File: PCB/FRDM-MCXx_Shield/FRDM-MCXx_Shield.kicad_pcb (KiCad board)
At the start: 4 copper layers, 54.3 x 54.7 mm, 96 parts, among them J1 Conn_02x08_Odd_Even, J2 Conn_02x06_Odd_Even, J3 Conn_02x10_Odd_Even, J4 Conn_02x08_Odd_Even, J5 Conn_01x04_Socket, J6 Conn_01x04_Pin, J7 Conn_01x04_Pin, J8 Conn_01x04_Pin, M1 Motor_Servo, SW1 EC12D1524406, U1 74HC595, U2 M95010-RMN6TP, U3 LM35-D

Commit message: Updated PCB
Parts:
- removed the REF2 at (73.8, 258.9)
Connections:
- J2 pad 2: /ADC_OUT -> /LM35_V_OUT
- U3 pad 1: /ADC_OUT -> /Sensors & actuators/LM35_V_OUT

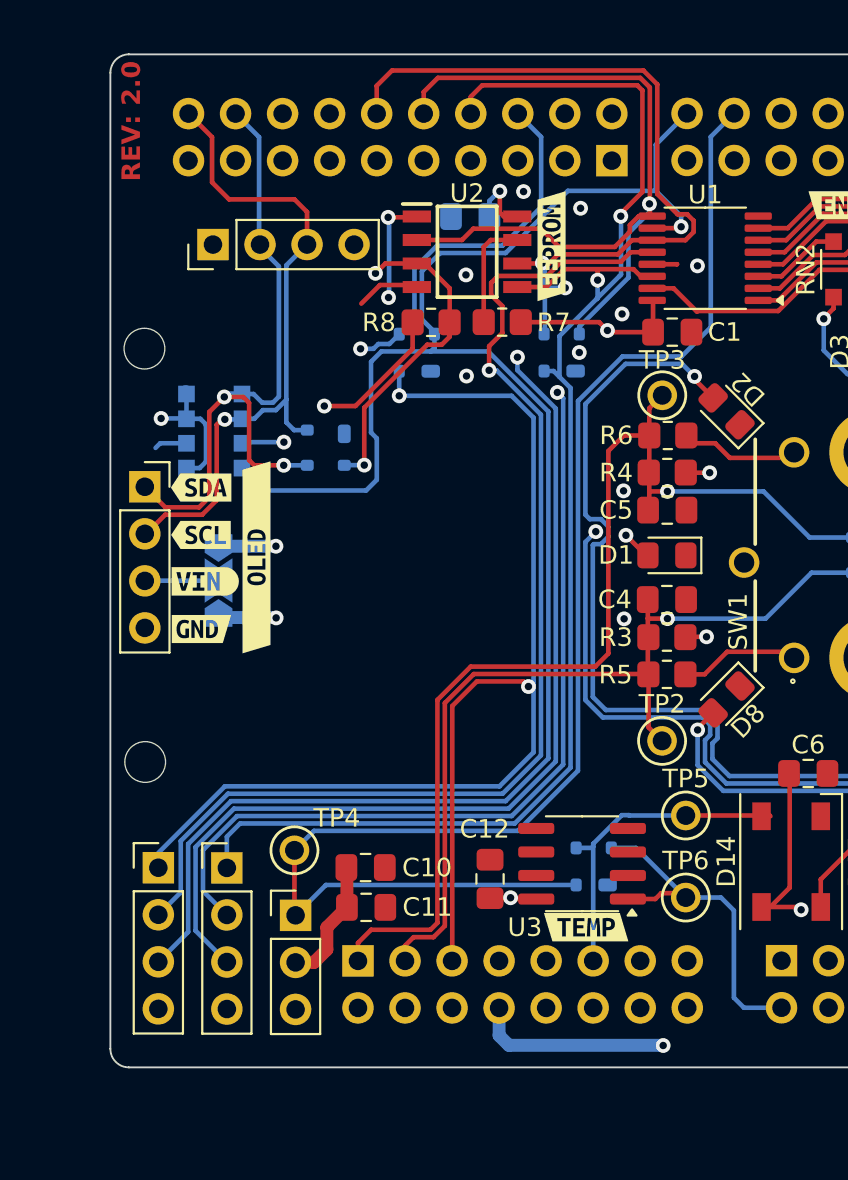
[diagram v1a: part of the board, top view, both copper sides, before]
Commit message: Updated labeling and header positions
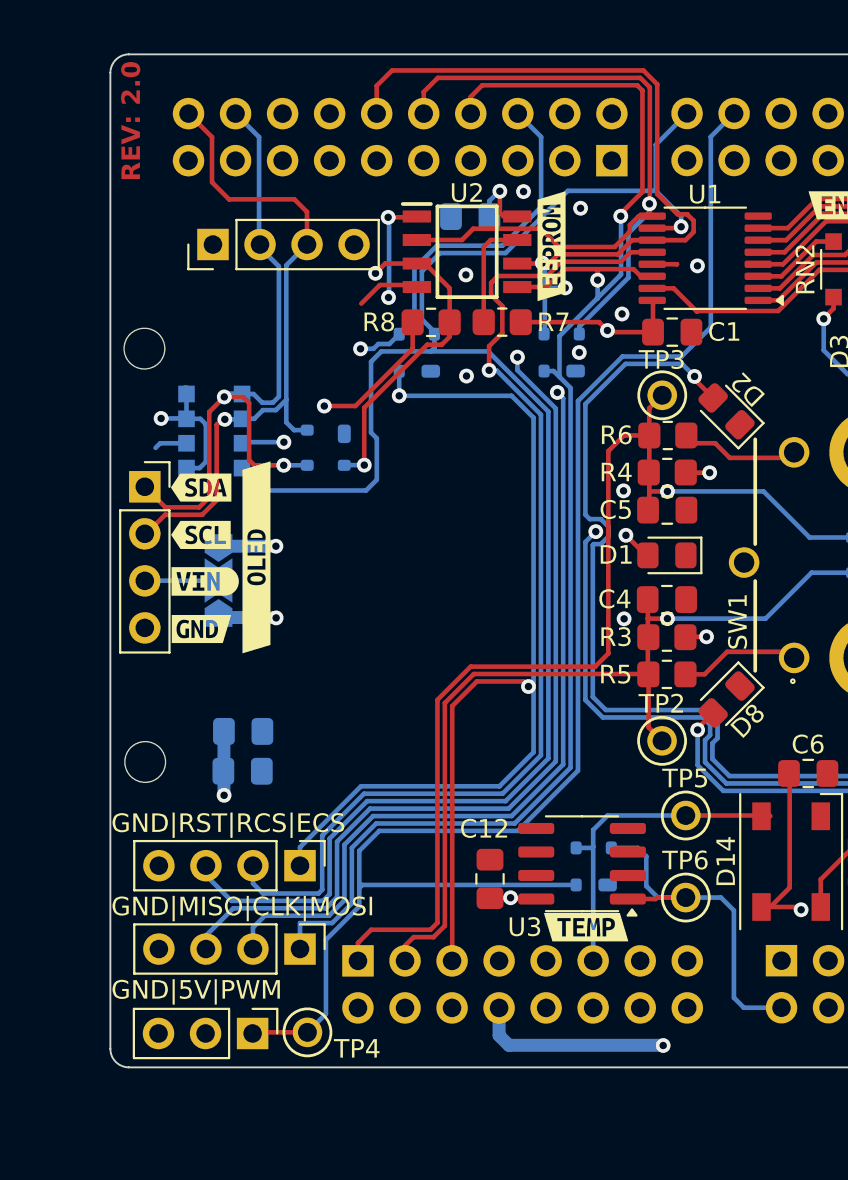
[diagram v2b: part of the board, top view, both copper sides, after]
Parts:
- removed kibuzzard-662F8C3C: G***, kibuzzard-662F8C3C
- removed kibuzzard-662F8C67: G***, kibuzzard-662F8C67
- removed kibuzzard-662FD263: G***, kibuzzard-662FD263
- removed kibuzzard-662FD313: G***, kibuzzard-662FD313
- C10, C11: moved to B.Cu
- moved C11 11.6 mm to (134.6, 100.5)
- moved TP4 9.85 mm to (138.1, 116.7), turned to -90 degrees
- moved C10 8.43 mm to (134.6, 102.6)
- moved J6 7.65 mm to (137.7, 107.7), turned to -90 degrees
- moved M1 6.79 mm to (135.1, 116.8), turned to -90 degrees
- moved J7 5.90 mm to (137.7, 112.2), turned to -90 degrees
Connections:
- D13 pad 4: /ADC_OUT -> /LM35_V_OUT
- TP6 pad 1: /ADC_OUT -> /LM35_V_OUT
- U3 pad 1: /Sensors & actuators/LM35_V_OUT -> /LM35_V_OUT
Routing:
- net /LM35_V_OUT: track 0.00 -> 19.6 mm
- net /ADC_OUT: track 18.8 -> 0.00 mm
- net /~{EEPROM_CS}: track 80.9 -> 73.3 mm
- net +5V: track 52.6 -> 59.2 mm, vias 1 -> 2
- net /~{SHIFTREG_CS}: track 107.1 -> 102.8 mm
- net /~{SHIFTREG_RST}: track 100.9 -> 97.0 mm
- net /SPI_MISO: track 107.9 -> 104.9 mm
- net /SERVO_PWM: track 77.3 -> 80.2 mm
- net /SPI_CLK: track 93.1 -> 91.0 mm
- net GND: track 8.20 -> 9.00 mm
- net /SPI_MOSI: track 81.7 -> 81.2 mm
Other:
- board text added: "ECS|RCS|RST|GND"
- board text added: "GND|5V|PWM"
- board text added: "GND|MISO|CLK|MOSI"
- board text added: "GND|RST|RCS|ECS"
- board text added: "MOSI|CLK|MISO|GND"
- board text added: "PWM|5V|GND"

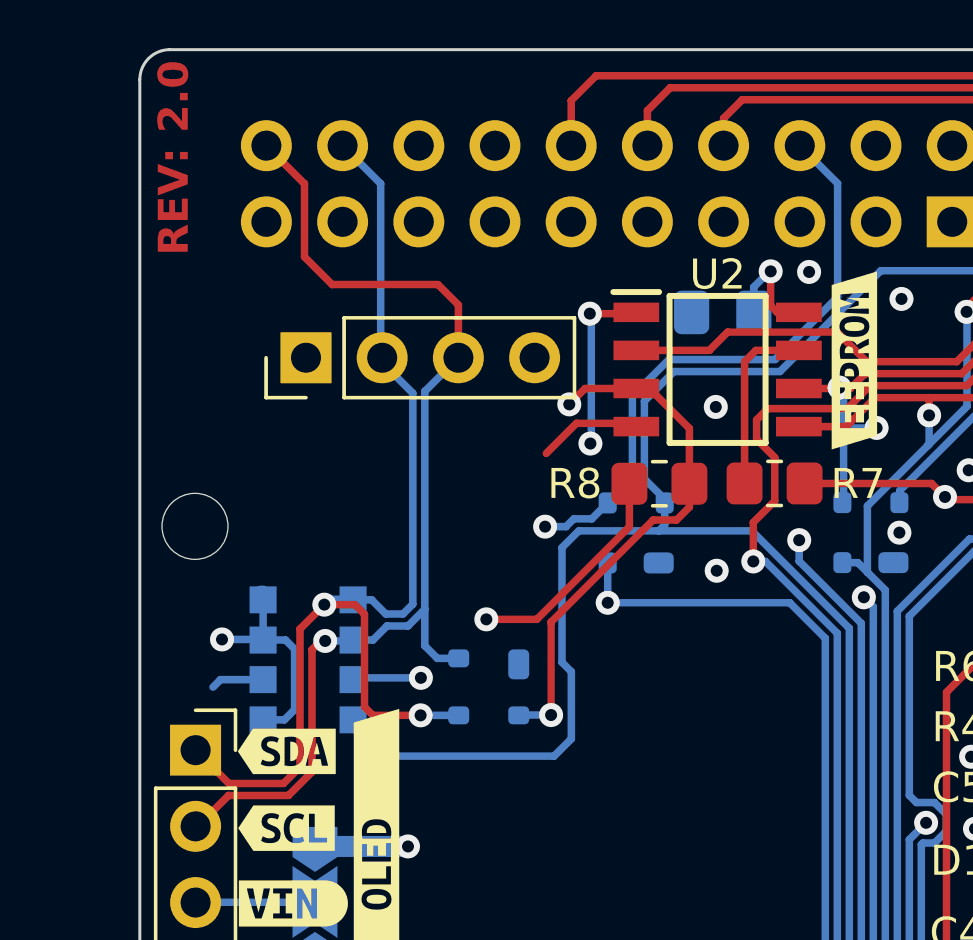
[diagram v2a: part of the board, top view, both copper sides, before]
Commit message: Added I2C header labels
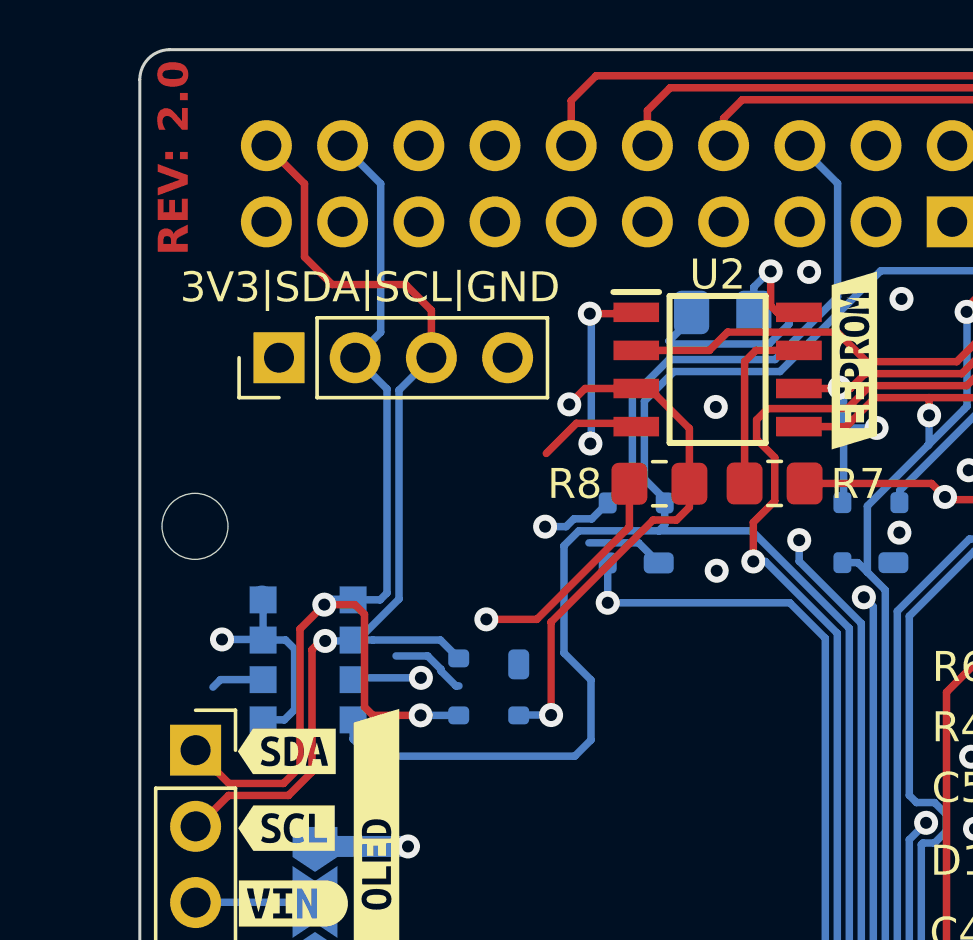
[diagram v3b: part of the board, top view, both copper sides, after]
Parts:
- moved J8 0.90 mm to (132.1, 74.2)
- moved kibuzzard-662EB4EE 0.90 mm to (135.7, 72.0)
- moved kibuzzard-662FE13B 0.90 mm to (137.2, 77.0)
- moved kibuzzard-662FE168 0.90 mm to (139.7, 77.0)
- moved kibuzzard-662FE170 0.90 mm to (132.1, 77.0)
- moved kibuzzard-662FE134 0.90 mm to (134.6, 77.0)
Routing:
- net GND: track 9.00 -> 19.8 mm
- net +3.3V: track 288.2 -> 290.2 mm
- net /~{SHIFTREG_RST}: track 97.0 -> 98.3 mm
- net /SDA: track 37.1 -> 36.0 mm
- net /SCL: track 36.4 -> 35.5 mm
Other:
- board text added: "3V3|SDA|SCL|GND"

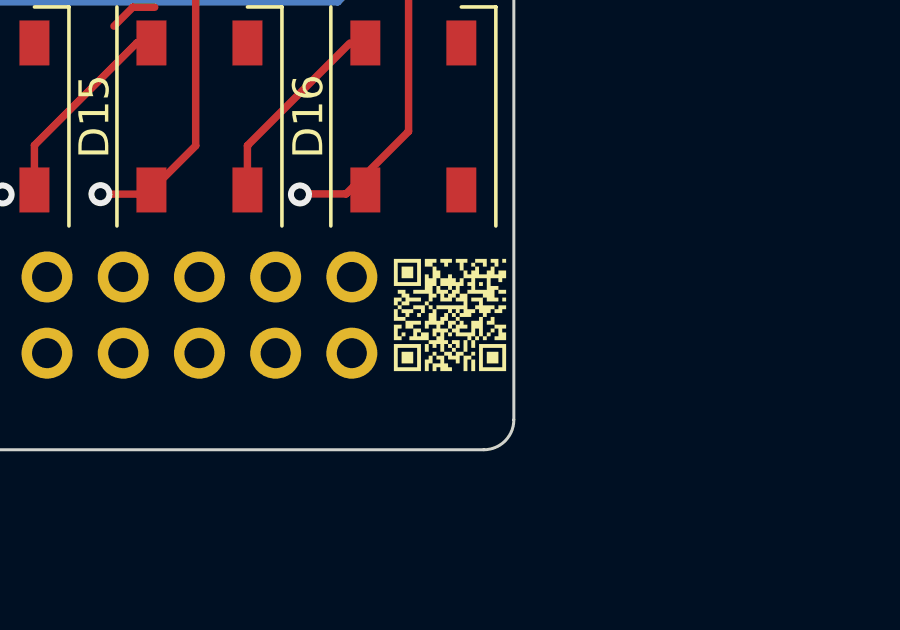
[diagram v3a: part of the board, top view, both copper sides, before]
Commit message: removed QR code
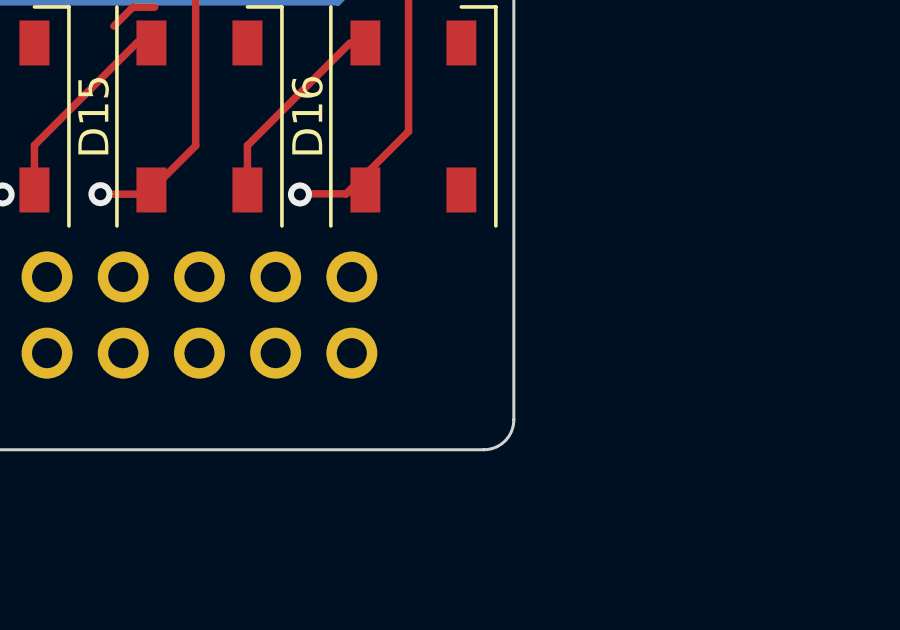
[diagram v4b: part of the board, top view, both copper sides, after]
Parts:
- removed the G*** at (179.7, 114.1)
- removed the G*** at (147.3, 91.3)

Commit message: Added easteregg
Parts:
- removed the G*** at (168.5, 90.9)
- added G***: LOGO, User:mandarij_proof_logo, F.Cu at (167.2, 90.8)
